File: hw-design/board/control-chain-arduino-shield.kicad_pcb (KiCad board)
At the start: 2 copper layers, 68.6 x 53.3 mm, 45 parts, among them J1 CC_INPUT, J2 CC_OUTPUT, P1 Power, P10 Power, P11 Analog, P12 Digital, P13 Digital, P2 Analog, P3 Digital, P4 Digital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

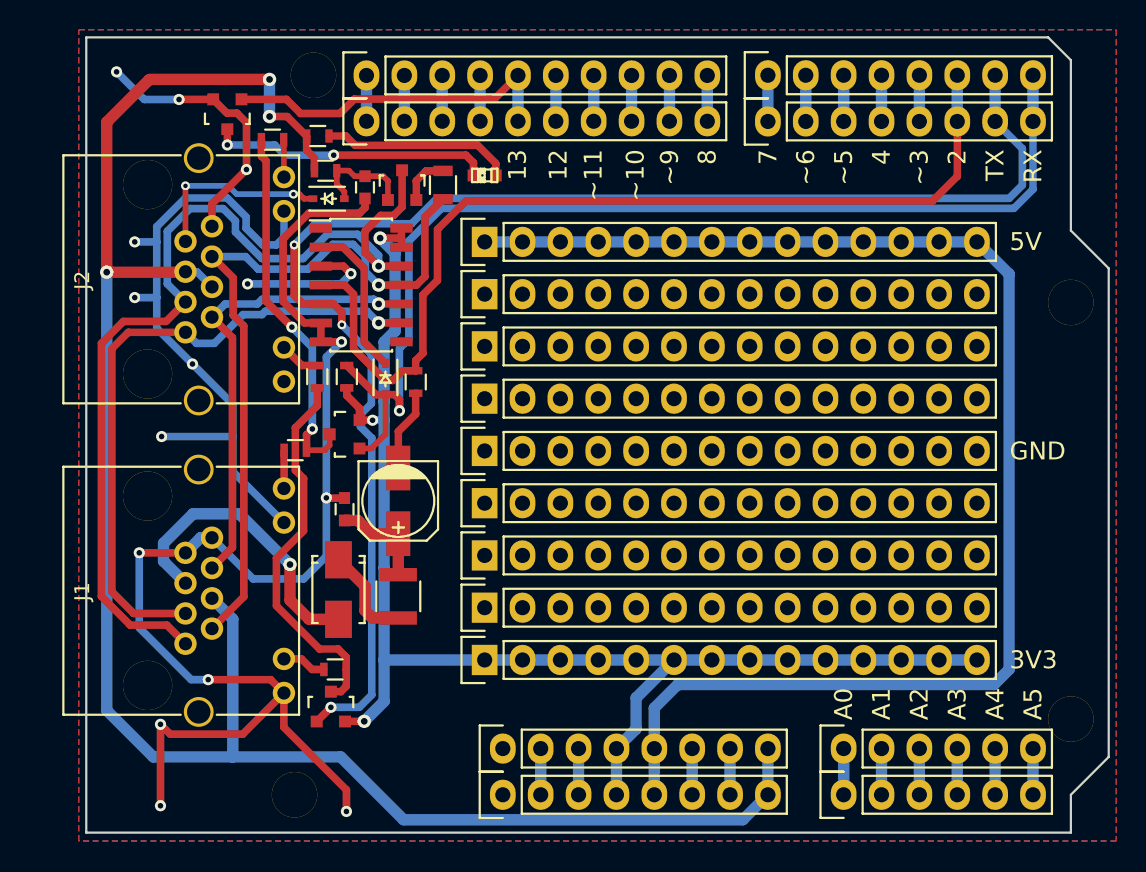
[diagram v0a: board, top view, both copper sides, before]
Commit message: improving silkscreen
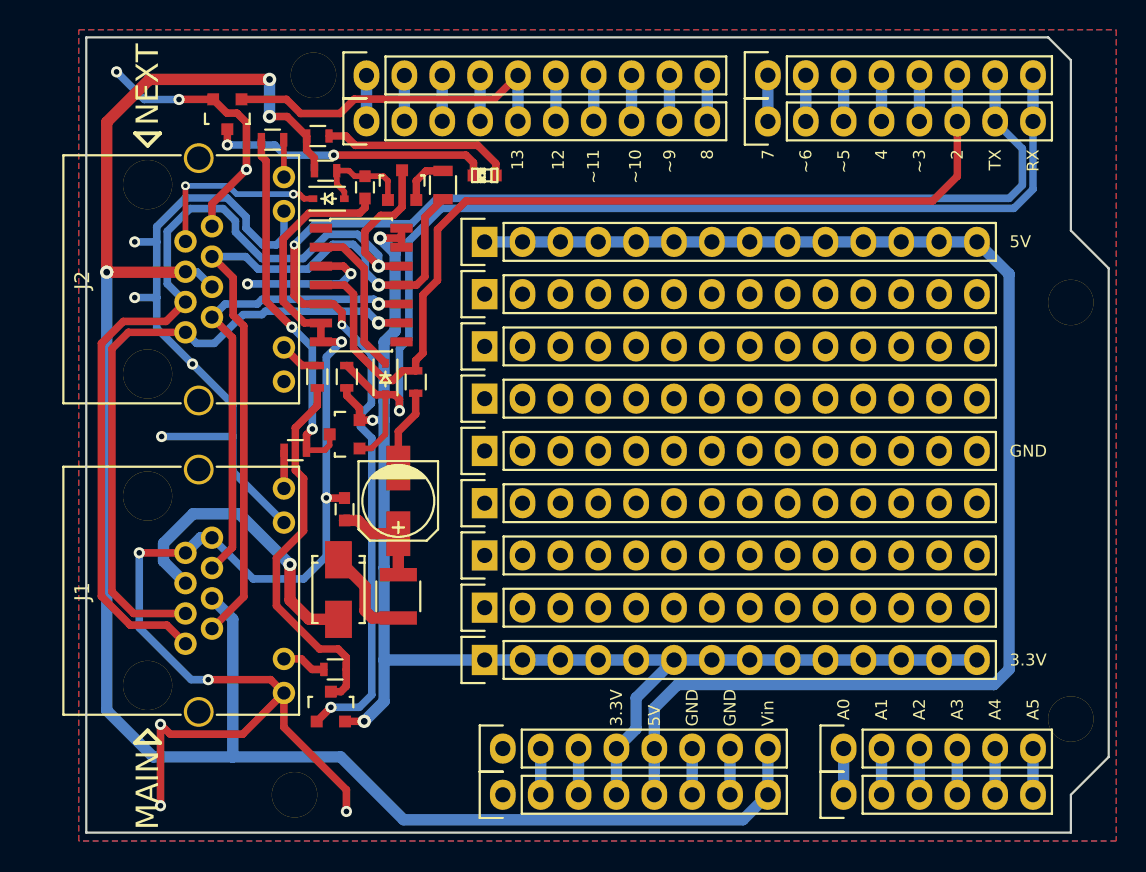
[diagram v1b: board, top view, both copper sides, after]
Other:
- board text added: "3.3V"
- board text added: "MAIN"
- board text added: "NEXT"
- board text added: "Vin"
- board text removed: "3V3"
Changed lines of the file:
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@@
     (area 110.922999 72.949999 179.653001 126.440001)
     (thickness 1.6)
-    (drawings 51)
+    (drawings 64)
     (tracks 441)
     (zones 0)
@@
     (pad "" thru_hole circle (at 0 0) (size 3.048 3.048) (drill 3.048) (layers *.Cu *.Mask F.SilkS))
   )
+  (gr_text 3.3V (at 146.558 119.23776 90) (layer F.SilkS)
+    (effects (font (size 0.8 0.8) (thickness 0.1)) (justify left))
+  )
+  (gr_text 5V (at 149.098 119.23776 90) (layer F.SilkS)
+    (effects (font (size 0.8 0.8) (thickness 0.1)) (justify left))
+  )
+  (gr_text Vin (at 156.718 119.23776 90) (layer F.SilkS)
+    (effects (font (size 0.8 0.8) (thickness 0.1)) (justify left))
+  )
+  (gr_text GND (at 151.638 119.23776 90) (layer F.SilkS)
+    (effects (font (size 0.8 0.8) (thickness 0.1)) (justify left))
+  )
+  (gr_text GND (at 154.178 119.23776 90) (layer F.SilkS)
+    (effects (font (size 0.8 0.8) (thickness 0.1)) (justify left))
+  )
+  (gr_text NEXT (at 115.10772 76.18476 90) (layer F.SilkS)
+    (effects (font (size 1.5 1.5) (thickness 0.3)))
+  )
+  (gr_line (start 115.11407 80.29829) (end 115.95735 79.45501) (angle 90) (layer F.SilkS) (width 0.254))
+  (gr_line (start 115.95735 79.45501) (end 114.27079 79.45501) (angle 90) (layer F.SilkS) (width 0.254))
+  (gr_line (start 114.27079 79.45501) (end 115.11407 80.29829) (angle 90) (layer F.SilkS) (width 0.254))
+  (gr_line (start 115.95608 120.3452) (end 115.1128 119.50192) (angle 90) (layer F.SilkS) (width 0.254))
+  (gr_line (start 114.26952 120.3452) (end 115.95608 120.3452) (angle 90) (layer F.SilkS) (width 0.254))
+  (gr_line (start 115.1128 119.50192) (end 114.26952 120.3452) (angle 90) (layer F.SilkS) (width 0.254))
+  (gr_text MAIN (at 115.1128 123.51258 90) (layer F.SilkS)
+    (effects (font (size 1.5 1.5) (thickness 0.3)))
+  )
   (dimension 53.416297 (width 0.3) (layer Dwgs.User)
     (gr_text "53.416 mm" (at 185.855482 99.668744 89.891021) (layer Dwgs.User)
@@
   )
   (gr_text A0 (at 161.798 118.8212 90) (layer F.SilkS)
-    (effects (font (size 1.2 1.2) (thickness 0.25)) (justify left))
+    (effects (font (size 0.8 0.8) (thickness 0.1)) (justify left))
   )
   (gr_text A1 (at 164.338 118.8212 90) (layer F.SilkS)
-    (effects (font (size 1.2 1.2) (thickness 0.25)) (justify left))
+    (effects (font (size 0.8 0.8) (thickness 0.1)) (justify left))
   )
   (gr_text A2 (at 166.878 118.8212 90) (layer F.SilkS)
-    (effects (font (size 1.2 1.2) (thickness 0.25)) (justify left))
+    (effects (font (size 0.8 0.8) (thickness 0.1)) (justify left))
   )
   (gr_text A3 (at 169.418 118.8212 90) (layer F.SilkS)
-    (effects (font (size 1.2 1.2) (thickness 0.25)) (justify left))
+    (effects (font (size 0.8 0.8) (thickness 0.1)) (justify left))
   )
   (gr_text A4 (at 171.958 118.8212 90) (layer F.SilkS)
-    (effects (font (size 1.2 1.2) (thickness 0.25)) (justify left))
+    (effects (font (size 0.8 0.8) (thickness 0.1)) (justify left))
   )
   (gr_text A5 (at 174.498 118.8212 90) (layer F.SilkS)
-    (effects (font (size 1.2 1.2) (thickness 0.25)) (justify left))
+    (effects (font (size 0.8 0.8) (thickness 0.1)) (justify left))
   )
   (gr_text 13 (at 139.9286 80.5307 90) (layer F.SilkS)
-    (effects (font (size 1.2 1.2) (thickness 0.25)) (justify right))
+    (effects (font (size 0.8 0.8) (thickness 0.1)) (justify right))
   )
   (gr_text 12 (at 142.6591 80.5307 90) (layer F.SilkS)
-    (effects (font (size 1.2 1.2) (thickness 0.25)) (justify right))
+    (effects (font (size 0.8 0.8) (thickness 0.1)) (justify right))
   )
   (gr_text ~~11 (at 145.0086 80.5307 90) (layer F.SilkS)
-    (effects (font (size 1.2 1.2) (thickness 0.25)) (justify right))
+    (effects (font (size 0.8 0.8) (thickness 0.1)) (justify right))
   )
   (gr_text ~~10 (at 147.828 80.5307 90) (layer F.SilkS)
-    (effects (font (size 1.2 1.2) (thickness 0.25)) (justify right))
+    (effects (font (size 0.8 0.8) (thickness 0.1)) (justify right))
   )
   (gr_text ~~9 (at 150.1267 80.5307 90) (layer F.SilkS)
-    (effects (font (size 1.2 1.2) (thickness 0.25)) (justify right))
+    (effects (font (size 0.8 0.8) (thickness 0.1)) (justify right))
   )
   (gr_text 8 (at 152.654 80.5307 90) (layer F.SilkS)
-    (effects (font (size 1.2 1.2) (thickness 0.25)) (justify right))
+    (effects (font (size 0.8 0.8) (thickness 0.1)) (justify right))
   )
   (gr_text 7 (at 156.7307 80.5307 90) (layer F.SilkS)
-    (effects (font (size 1.2 1.2) (thickness 0.25)) (justify right))
+    (effects (font (size 0.8 0.8) (thickness 0.1)) (justify right))
   )
   (gr_text ~~6 (at 159.258 80.5307 90) (layer F.SilkS)
-    (effects (font (size 1.2 1.2) (thickness 0.25)) (justify right))
+    (effects (font (size 0.8 0.8) (thickness 0.1)) (justify right))
   )
   (gr_text ~~5 (at 161.798 80.5307 90) (layer F.SilkS)
-    (effects (font (size 1.2 1.2) (thickness 0.25)) (justify right))
+    (effects (font (size 0.8 0.8) (thickness 0.1)) (justify right))
   )
   (gr_text 4 (at 164.338 80.5307 90) (layer F.SilkS)
-    (effects (font (size 1.2 1.2) (thickness 0.25)) (justify right))
+    (effects (font (size 0.8 0.8) (thickness 0.1)) (justify right))
   )
   (gr_text ~~3 (at 166.878 80.5307 90) (layer F.SilkS)
-    (effects (font (size 1.2 1.2) (thickness 0.25)) (justify right))
+    (effects (font (size 0.8 0.8) (thickness 0.1)) (justify right))
   )
   (gr_text 2 (at 169.418 80.5307 90) (layer F.SilkS)
-    (effects (font (size 1.2 1.2) (thickness 0.25)) (justify right))
+    (effects (font (size 0.8 0.8) (thickness 0.1)) (justify right))
   )
   (gr_text TX (at 171.958 80.5307 90) (layer F.SilkS)
-    (effects (font (size 1.2 1.2) (thickness 0.25)) (justify right))
+    (effects (font (size 0.8 0.8) (thickness 0.1)) (justify right))
   )
   (gr_text RX (at 174.498 80.5307 90) (layer F.SilkS)
-    (effects (font (size 1.2 1.2) (thickness 0.25)) (justify right))
-  )
-  (gr_text 3V3 (at 172.9232 114.7826) (layer F.SilkS)
-    (effects (font (size 1.2 1.2) (thickness 0.25)) (justify left))
+    (effects (font (size 0.8 0.8) (thickness 0.1)) (justify right))
+  )
+  (gr_text 3.3V (at 172.9232 114.7826) (layer F.SilkS)
+    (effects (font (size 0.8 0.8) (thickness 0.1)) (justify left))
   )
   (gr_text GND (at 172.9232 100.7745) (layer F.SilkS)
-    (effects (font (size 1.2 1.2) (thickness 0.25)) (justify left))
+    (effects (font (size 0.8 0.8) (thickness 0.1)) (justify left))
   )
   (gr_text 5V (at 172.9232 86.7283) (layer F.SilkS)
-    (effects (font (size 1.2 1.2) (thickness 0.25)) (justify left))
+    (effects (font (size 0.8 0.8) (thickness 0.1)) (justify left))
   )
   (gr_circle (center 117.348 76.962) (end 118.618 76.962) (layer Dwgs.User) (width 0.15))

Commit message: fixing user led voltage
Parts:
- R1: value 1K -> 330R
- moved R9 0.19 mm to (135.1, 82.9)
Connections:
- R1 pad 1: +12V -> +3V3
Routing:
- net +3V3: track 92.3 -> 106.9 mm, vias 3 -> 5
- net Net-(Q4-Pad2): track 3.36 -> 3.93 mm, vias 0 -> 2

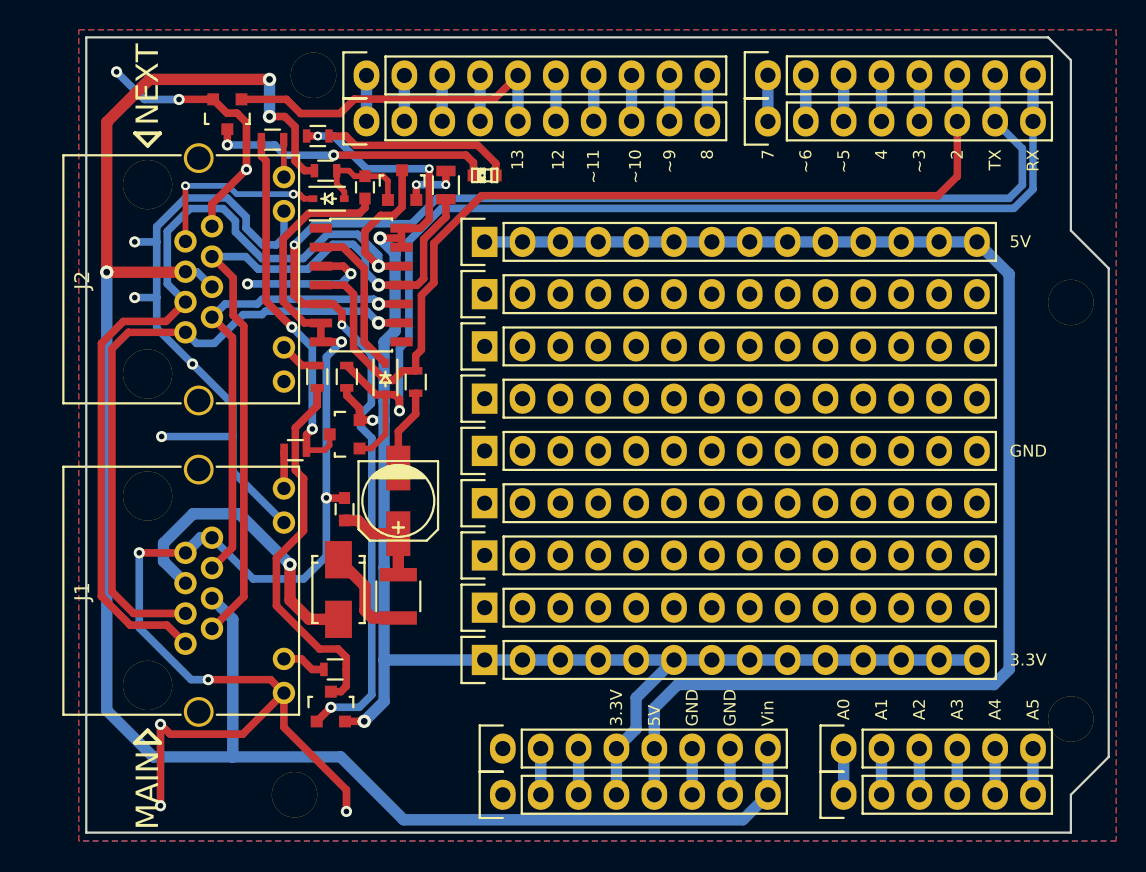
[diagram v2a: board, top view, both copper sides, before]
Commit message: update layout to last schematic
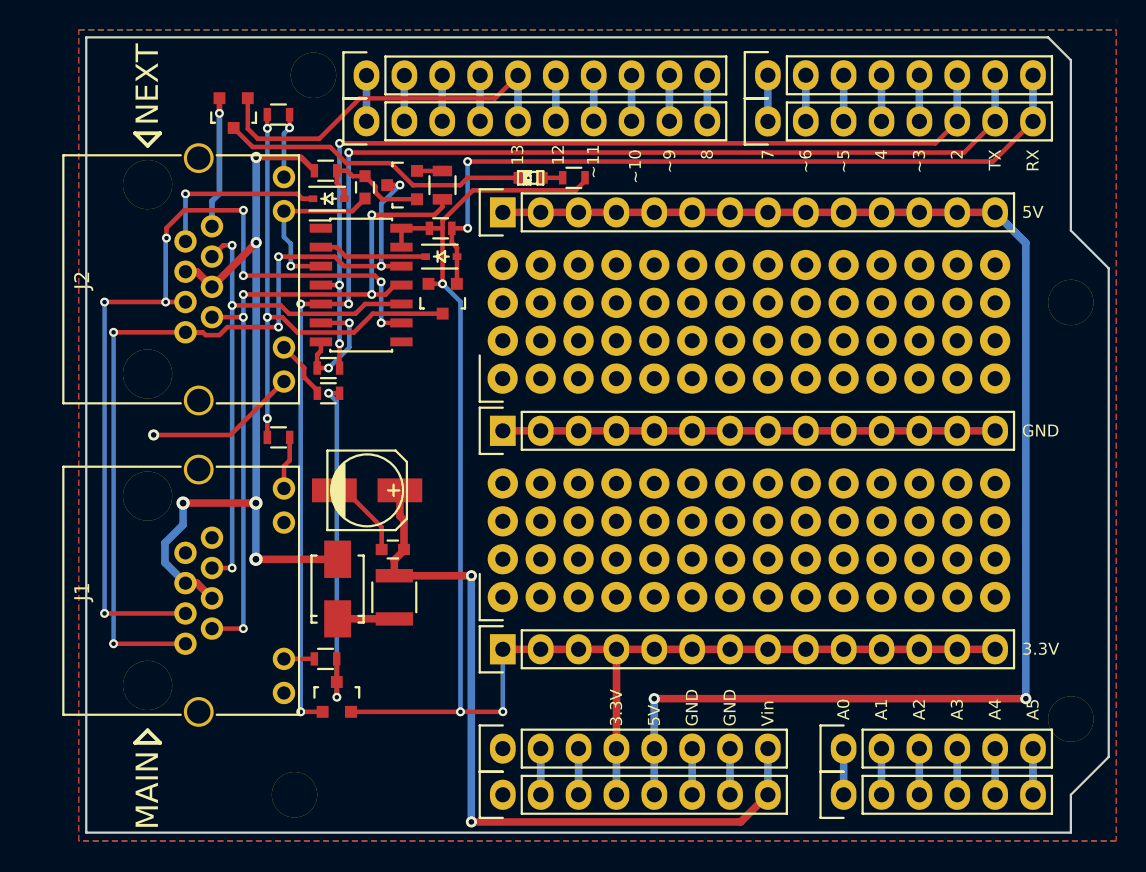
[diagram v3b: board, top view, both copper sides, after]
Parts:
- removed P15, P16, P17, P18: ~, Pin_Headers:Pin_Header_Straight_1x14
- J1: value CC_INPUT -> CC_MAIN
- J2: value CC_OUTPUT -> CC_NEXT
- P14, P9: footprint Pin_Headers:Pin_Header_Straight_1x14 -> Socket_Arduino_Uno:Perfboard
- moved R1 17.4 mm to (143.7, 82.4), turned to 180 degrees
- moved R11 11.8 mm to (134.8, 85.8), turned to 0 degrees
- moved Q2 11.2 mm to (134.9, 90.6), turned to 180 degrees
- moved D4 9.02 mm to (134.8, 87.7), turned to 0 degrees
- moved P9 6.41 mm to (138.9, 110.6)
- moved R10 5.93 mm to (127.2, 95.2), turned to 0 degrees
- moved C2 4.22 mm to (131.6, 107.4), turned to 180 degrees
- moved D2 3.09 mm to (140.8, 82.4)
- moved P20 2.32 mm to (138.9, 84.8)
- moved C1 2.21 mm to (129.8, 103.4), turned to 0 degrees
- moved P21 1.82 mm to (138.9, 99.4)
- moved P14 1.82 mm to (138.9, 95.9)
- moved R4 1.73 mm to (123.9, 78.2)
- moved R2 1.42 mm to (123.9, 99.9), turned to 180 degrees
- moved P19 1.41 mm to (138.9, 114.1)
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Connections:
- D1 pad 2: POWER_INPUT -> +12V
- J1 pad 5: POWER_INPUT -> +12V
- J2 pad 1: RS485_TX+ -> RS485_RX+
- J2 pad 2: RS485_TX- -> RS485_RX-
- J2 pad 3: RS485_RX+ -> RS485_TX+
- J2 pad 6: RS485_RX- -> RS485_TX-
- P1 pad 8: +12V -> VIN
- P10 pad 8: +12V -> VIN
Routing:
- net GNDD: track 176.7 -> 86.8 mm, vias 16 -> 5
- net +12V: track 130.2 -> 56.8 mm, vias 3 -> 5
- net VIN: track 6.73 -> 51.5 mm, vias 0 -> 2
- net IO0/RXD: track 72.6 -> 51.5 mm, vias 1 -> 2
- net POWER_INPUT: track 20.2 -> 0.00 mm, vias 1 -> 0
- net RS485_TX+: track 43.2 -> 60.3 mm, vias 1 -> 8
- net Net-(D2-Pad2): track 12.8 -> 1.40 mm
- net RS485_RX_LED: track 24.8 -> 34.4 mm, vias 2 -> 3
- net IO1/TXD: track 97.2 -> 89.6 mm, vias 3 -> 4
- net +5V: track 93.3 -> 100.8 mm, vias 0 -> 2
- net RS485_RX+: track 64.5 -> 59.1 mm, vias 1 -> 6
- net RS485_TX-: track 31.3 -> 36.5 mm, vias 1 -> 3
- net Net-(D4-Pad1): track 10.4 -> 7.28 mm
- net Net-(D1-Pad1): track 6.59 -> 3.81 mm
- net IO2: track 64.2 -> 61.5 mm, vias 0 -> 3
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
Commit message: change RJ45 connector
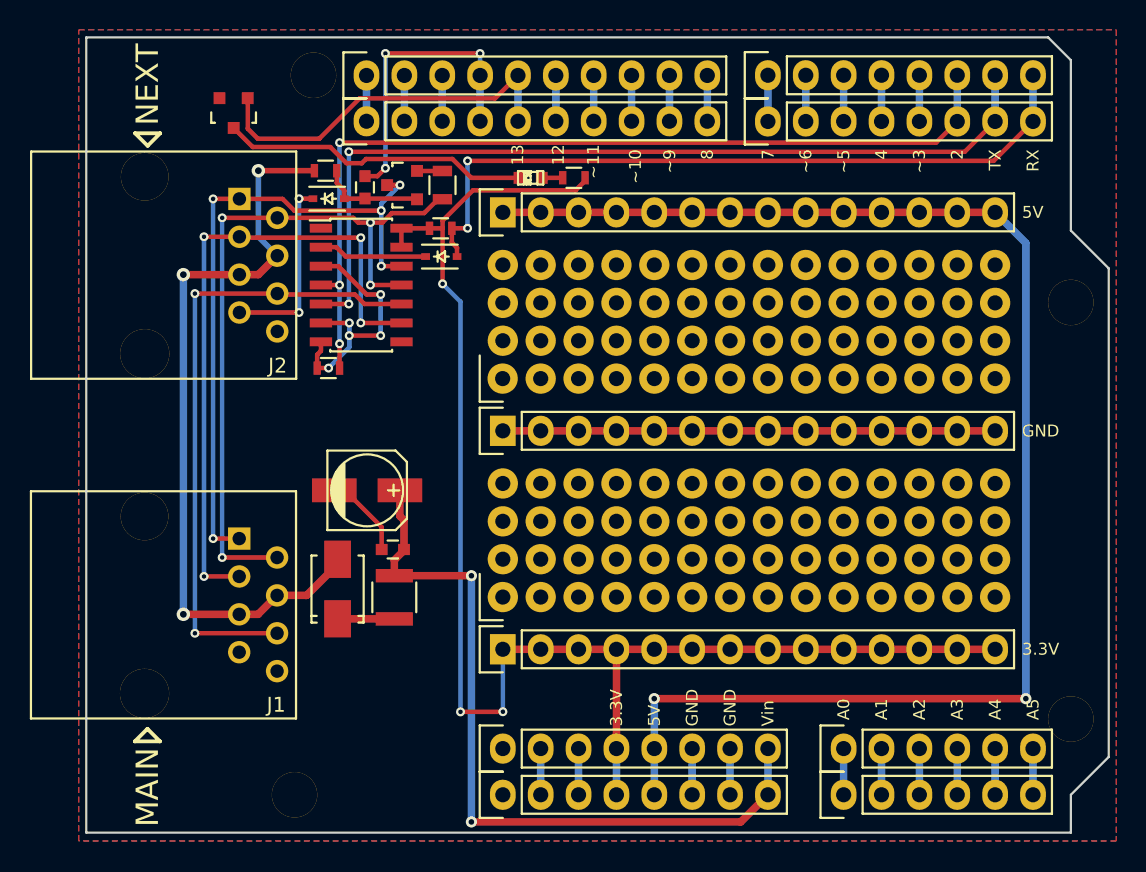
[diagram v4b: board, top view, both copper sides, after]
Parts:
- removed Q2, Q3: BSS84, Housings_SOT-23_SOT-143_TSOT-6:SOT-23
- removed R2, R3, R4, R5: 330R, Resistors_SMD:R_0603
- J1, J2: footprint Connect:RJHSE538X -> local-footprints:54602-908LF
- moved J2 9.65 mm to (121.3, 83.9), turned to 270 degrees
- moved J1 7.92 mm to (121.3, 106.6), turned to 270 degrees
- turned C3 to 90 degrees
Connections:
- P1 pad 1: Net-(P1-Pad1) -> (no net)
- P10 pad 1: Net-(P10-Pad1) -> (no net)
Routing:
- net RS485_RX_LED: track 34.4 -> 0.00 mm, vias 3 -> 0
- net IO1/TXD: track 89.6 -> 59.4 mm, vias 4 -> 2
- net RS485_TX_LED: track 23.9 -> 0.00 mm, vias 2 -> 0
- net RS485_TX+: track 60.3 -> 44.1 mm, vias 8 -> 4
- net RS485_RX+: track 59.1 -> 45.2 mm, vias 6 -> 5
- net +3V3: track 106.7 -> 98.4 mm
- net RS485_TX-: track 36.5 -> 42.4 mm, vias 3 -> 2
- net +12V: track 56.8 -> 51.9 mm, vias 5 -> 3
- net Net-(J2-Pad12): track 4.35 -> 0.00 mm, vias 1 -> 0
- net Net-(J2-Pad10): track 3.99 -> 0.00 mm
- net GNDD: track 86.8 -> 82.9 mm, vias 5 -> 8
- net Net-(J1-Pad12): track 3.59 -> 0.00 mm
- net +5V: track 100.8 -> 97.9 mm
- net Net-(J1-Pad10): track 2.04 -> 0.00 mm
- net IO0/RXD: track 51.5 -> 49.7 mm
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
